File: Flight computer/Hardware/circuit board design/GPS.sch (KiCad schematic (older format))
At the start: 5 parts, among them U12 MAX2659ELT+, U13 SAFEB1G57KE0F00, U4 MAX-M8C

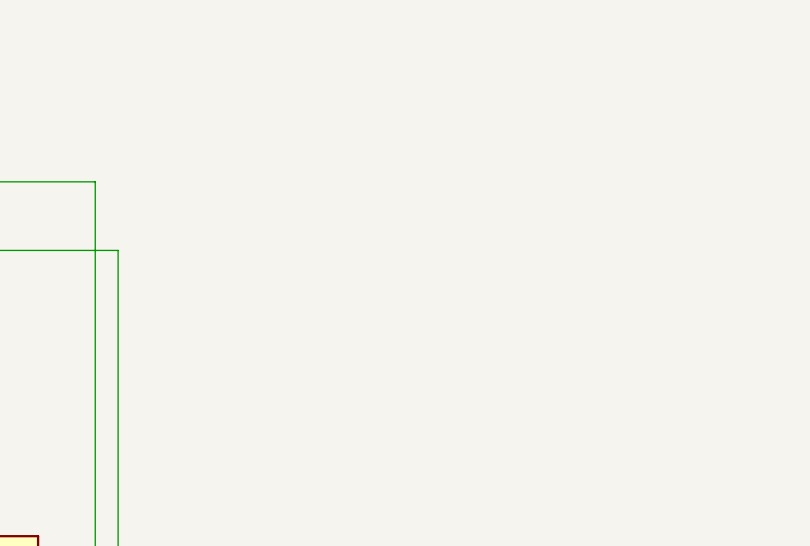
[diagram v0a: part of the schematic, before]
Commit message: moved gps antenna coax connection to right page
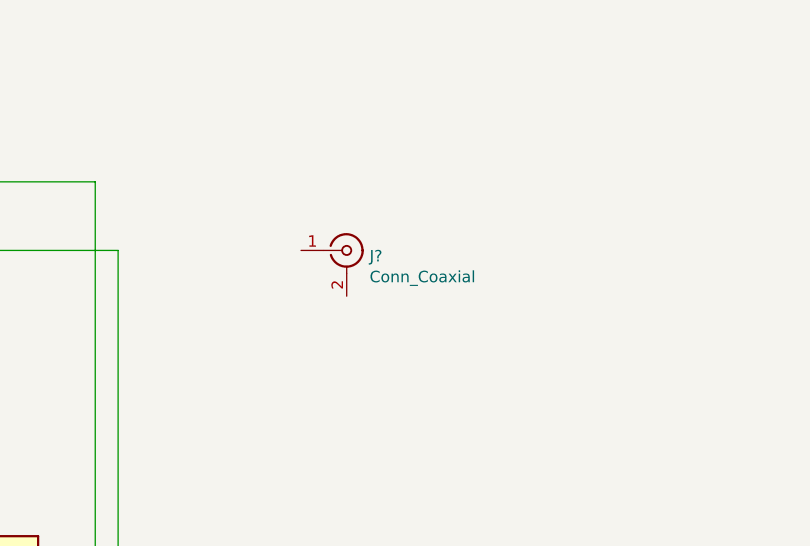
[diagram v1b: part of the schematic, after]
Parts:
- added J?: Conn_Coaxial, Connector_Coaxial:U.FL_Hirose_U.FL-R-SMT-1_Vertical, symbol Connector:Conn_Coaxial
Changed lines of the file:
@@
 Wire Wire Line
 	1800 1900 2100 1900
+$Comp
+L Connector:Conn_Coaxial J?
+U 1 1 5D772D40
+P 7900 2200
+AR Path="/5D5B17D8/5D772D40" Ref="J?"  Part="1"
+AR Path="/5D5B165E/5D772D40" Ref="J?"  Part="1"
+F 0 "J?" H 8000 2175 50  0000 L CNN
+F 1 "Conn_Coaxial" H 8000 2084 50  0000 L CNN
+F 2 "Connector_Coaxial:U.FL_Hirose_U.FL-R-SMT-1_Vertical" H 7900 2200 50  0001 C CNN
+F 3 " ~" H 7900 2200 50  0001 C CNN
+	1    7900 2200
+	1    0    0    -1
+$EndComp
 $EndSCHEMATC

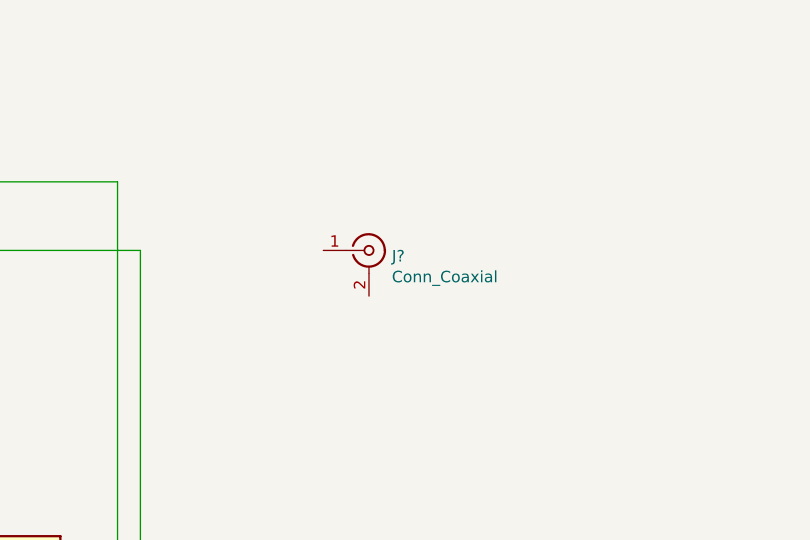
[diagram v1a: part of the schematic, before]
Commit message: added in the RF front end, exactly as stated in AN904
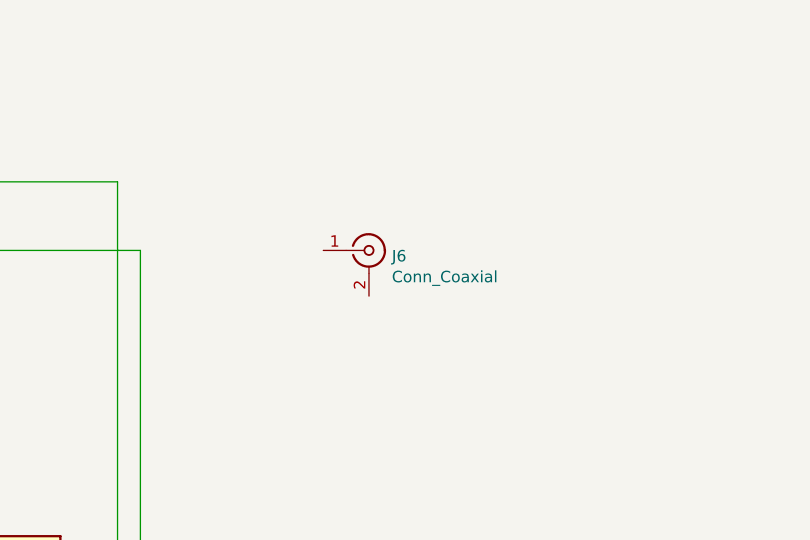
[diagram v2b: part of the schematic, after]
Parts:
- gave numbers to parts that had none: 1
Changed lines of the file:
@@
 P 7900 2200
 AR Path="/5D5B17D8/5D772D40" Ref="J?"  Part="1"
-AR Path="/5D5B165E/5D772D40" Ref="J?"  Part="1"
-F 0 "J?" H 8000 2175 50  0000 L CNN
+AR Path="/5D5B165E/5D772D40" Ref="J6"  Part="1"
+F 0 "J6" H 8000 2175 50  0000 L CNN
 F 1 "Conn_Coaxial" H 8000 2084 50  0000 L CNN
 F 2 "Connector_Coaxial:U.FL_Hirose_U.FL-R-SMT-1_Vertical" H 7900 2200 50  0001 C CNN

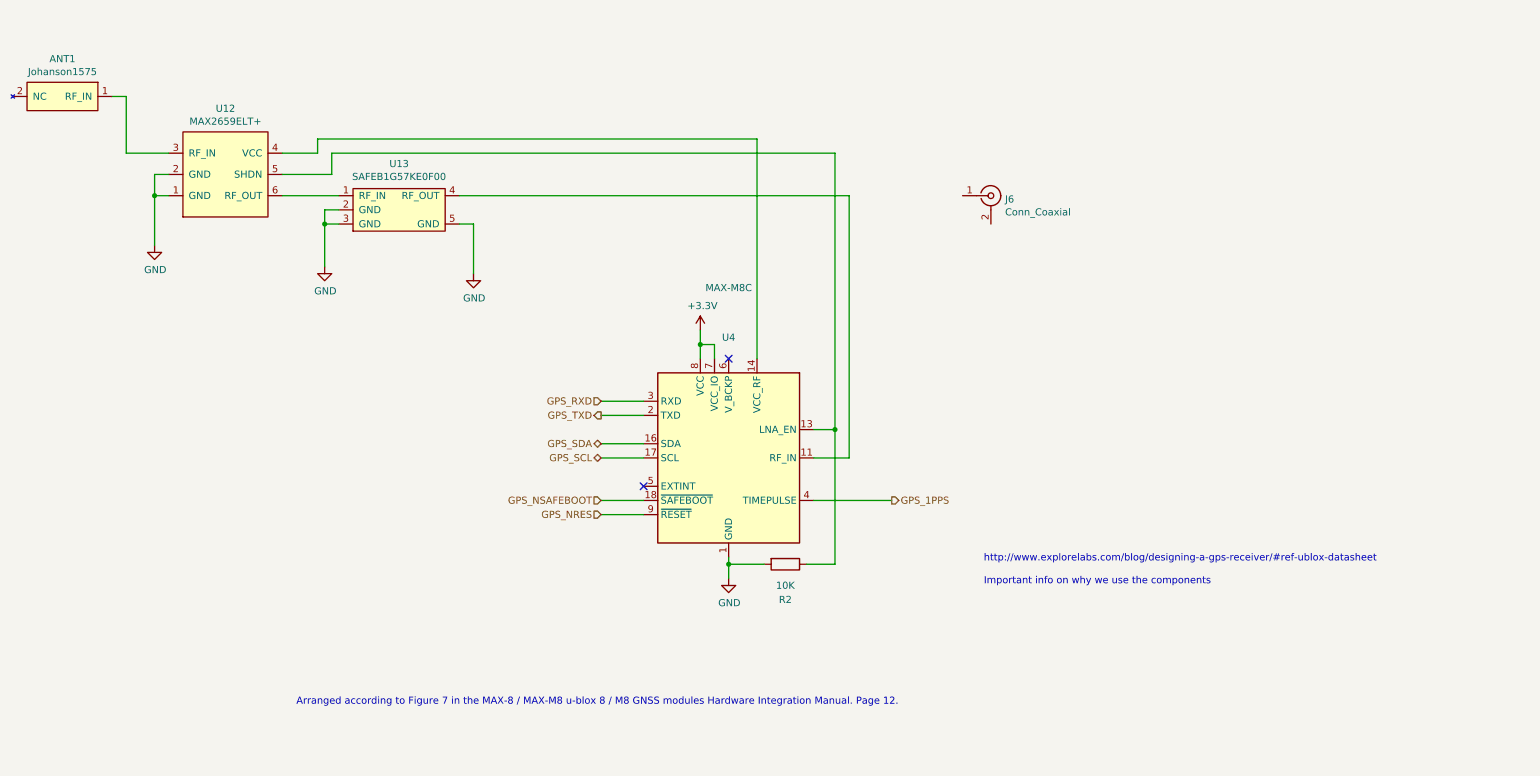
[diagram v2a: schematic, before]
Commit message: put in a UFL connector in place of the Active GPS antenna
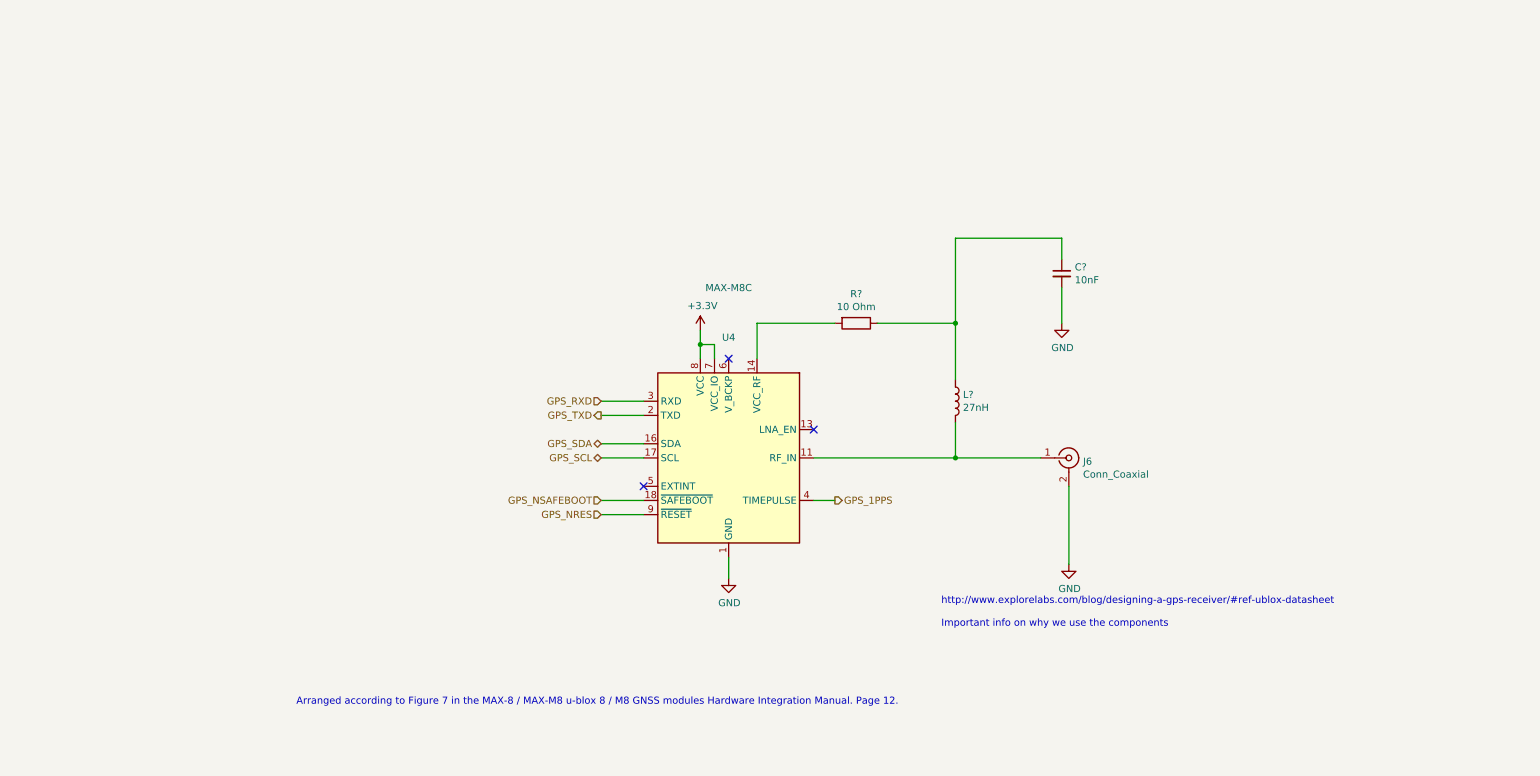
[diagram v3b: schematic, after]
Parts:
- removed ANT1: Johanson1575, pico_tracker:Johanson1575, symbol flight-computer:ICSSPicoTracker_Johanson1575
- removed R2: 10K, Resistor_SMD:R_0603_1608Metric, symbol Device:R
- removed U12: MAX2659ELT+, pico_tracker:uDFN-6_1.0x1.5mm_P0.5mm, symbol flight-computer:ICSSPicoTracker_MAX2659ELT+
- removed U13: SAFEB1G57KE0F00, pico_tracker:Murata SAFE, symbol flight-computer:ICSSPicoTracker_SAFEB1G57KE0F00
- added C?: 10nF, symbol Device:C_Small
- added L?: 27nH, symbol Device:L
- added R?: 10 Ohm, symbol Device:R
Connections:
- net GND: now also J6.2 (Ext), C?.2
- net at U4.14 (VCC_RF): now also R?.2
- net at U4.11 (RF_IN): now also J6.1 (In), L?.2
- new net: C?.1, L?.1, R?.1
- no-connect marks 2 -> 3
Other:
- moved on the sheet: J6
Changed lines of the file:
@@
 Comment4 ""
 $EndDescr
+Text HLabel 6800 4350 2    50   Output ~ 0
+GPS_1PPS
+Text Notes 3000 5800 0    50   ~ 0
+Arranged according to Figure 7 in the MAX-8 / MAX-M8 u-blox 8 / M8 GNSS modules Hardware Integration Manual. Page 12.
+Text Notes 7550 5250 0    50   ~ 0
+http://www.explorelabs.com/blog/designing-a-gps-receiver/#ref-ublox-datasheet\n\nImportant info on why we use the components\n
 $Comp
-L flight-computer:ICSSPicoTracker_SAFEB1G57KE0F00 U13
-U 1 1 5D44BB5C
-P 3400 2450
-F 0 "U13" H 3725 2925 50  0000 C CNN
-F 1 "SAFEB1G57KE0F00" H 3725 2834 50  0000 C CNN
-F 2 "pico_tracker:Murata SAFE" H 3400 2450 50  0001 C CNN
-F 3 "https://www.murata.com/en-eu/products/productdata/8797690593310/DS-SAFEB1G57KE0F00.pdf?1453347007000" H 3400 2450 50  0001 C CNN
-F 4 "https://www.rf-microwave.com/en/murata/safeb1g57ke0f00/1575-5-mhz-band-pass-saw/fw-safeb1g57/" H 3400 2450 50  0001 C CNN "Purchase link"
-	1    3400 2450
+L power:+3.3V #PWR010
+U 1 1 5D692740
+P 5850 3150
+F 0 "#PWR010" H 5850 3000 50  0001 C CNN
+F 1 "+3.3V" H 5865 3323 50  0000 C CNN
+F 2 "" H 5850 3150 50  0001 C CNN
+F 3 "" H 5850 3150 50  0001 C CNN
+	1    5850 3150
 	1    0    0    -1
 $EndComp
 $Comp
-L power:GND #PWR053
-U 1 1 5D459323
-P 3200 2700
-F 0 "#PWR053" H 3200 2450 50  0001 C CNN
-F 1 "GND" H 3205 2527 50  0000 C CNN
-F 2 "" H 3200 2700 50  0001 C CNN
-F 3 "" H 3200 2700 50  0001 C CNN
-	1    3200 2700
-	1    0    0    -1
-$EndComp
-$Comp
-L power:GND #PWR058
-U 1 1 5D459A04
-P 4250 2750
-F 0 "#PWR058" H 4250 2500 50  0001 C CNN
-F 1 "GND" H 4255 2577 50  0000 C CNN
-F 2 "" H 4250 2750 50  0001 C CNN
-F 3 "" H 4250 2750 50  0001 C CNN
-	1    4250 2750
+L power:GND #PWR011
+U 1 1 5D67FE0F
+P 6050 4900
+F 0 "#PWR011" H 6050 4650 50  0001 C CNN
+F 1 "GND" H 6055 4727 50  0000 C CNN
+F 2 "" H 6050 4900 50  0001 C CNN
+F 3 "" H 6050 4900 50  0001 C CNN
+	1    6050 4900
 	1    0    0    -1
 $EndComp
 Wire Wire Line
-	4150 2400 4250 2400
+	5850 3150 5850 3250
 Wire Wire Line
-	4250 2400 4250 2750
+	5950 3250 5850 3250
+Text HLabel 5150 3750 0    50   Output ~ 0
+GPS_TXD
+Text HLabel 5150 3650 0    50   Input ~ 0
+GPS_RXD
+Text HLabel 5150 4050 0    50   BiDi ~ 0
+GPS_SCL
+Text HLabel 5150 3950 0    50   BiDi ~ 0
+GPS_SDA
+Text HLabel 5150 4350 0    50   Input ~ 0
+GPS_NSAFEBOOT
+Text HLabel 5150 4450 0    50   Input ~ 0
+GPS_NRES
+$Comp
+L Connector:Conn_Coaxial J?
+U 1 1 5D772D40
+P 8450 4050
+AR Path="/5D5B17D8/5D772D40" Ref="J?"  Part="1"
+AR Path="/5D5B165E/5D772D40" Ref="J6"  Part="1"
+F 0 "J6" H 8550 4025 50  0000 L CNN
+F 1 "Conn_Coaxial" H 8550 3934 50  0000 L CNN
+F 2 "Connector_Coaxial:U.FL_Hirose_U.FL-R-SMT-1_Vertical" H 8450 4050 50  0001 C CNN
+F 3 " ~" H 8450 4050 50  0001 C CNN
+	1    8450 4050
+	1    0    0    -1
+$EndComp
 Wire Wire Line
-	3300 2300 3200 2300
+	8450 4800 8450 4250
+$Comp
+L power:GND #PWR?
+U 1 1 5D7B7248
+P 8450 4800
+F 0 "#PWR?" H 8450 4550 50  0001 C CNN
+F 1 "GND" H 8455 4627 50  0000 C CNN
+F 2 "" H 8450 4800 50  0001 C CNN
+F 3 "" H 8450 4800 50  0001 C CNN
+	1    8450 4800
+	1    0    0    -1
+$EndComp
+Connection ~ 7650 4050
 Wire Wire Line
-	3200 2300 3200 2400
+	7650 4050 8250 4050
+$Comp
+L Device:L L?
+U 1 1 5D7B7FB8
+P 7650 3650
+F 0 "L?" H 7703 3696 50  0000 L CNN
+F 1 "27nH" H 7703 3605 50  0000 L CNN
+F 2 "" H 7650 3650 50  0001 C CNN
+F 3 "~" H 7650 3650 50  0001 C CNN
+	1    7650 3650
+	1    0    0    -1
+$EndComp
 Wire Wire Line
-	3300 2400 3200 2400
-Connection ~ 3200 2400
+	7650 3800 7650 4050
+Connection ~ 5850 3250
 Wire Wire Line
-	3200 2400 3200 2700
+	5150 4450 5450 4450
 Wire Wire Line
-	3250 2050 3250 1900
-Text HLabel 7200 4350 2    50   Output ~ 0
-GPS_1PPS
-Text Notes 3000 5800 0    50   ~ 0
-Arranged according to Figure 7 in the MAX-8 / MAX-M8 u-blox 8 / M8 GNSS modules Hardware Integration Manual. Page 12.
+	5850 3250 5850 3350
 Wire Wire Line
-	3250 1900 6800 1900
-Text Notes 7850 4950 0    50   ~ 0
-http://www.explorelabs.com/blog/designing-a-gps-receiver/#ref-ublox-datasheet\n\nImportant info on why we use the components\n
+	5950 3350 5950 3250
+NoConn ~ 6050 3350
 NoConn ~ 5450 4250
+Wire Wire Line
+	6650 4350 6800 4350
+Wire Wire Line
+	5450 3650 5150 3650
+Wire Wire Line
+	5150 3750 5450 3750
+Wire Wire Line
+	5450 4350 5150 4350
+Wire Wire Line
+	5150 4050 5450 4050
+Wire Wire Line
+	5450 3950 5150 3950
+NoConn ~ 6650 3850
+Wire Wire Line
+	6650 4050 7650 4050
+Wire Wire Line
+	6050 4750 6050 4900
 $Comp
 L RF_GPS:MAX-M8C U4
@@
 $EndComp
 Wire Wire Line
-	6300 4800 6050 4800
+	6250 3350 6250 3100
+Wire Wire Line
+	6250 3100 6800 3100
+Wire Wire Line
+	7650 3100 7650 3500
 $Comp
-L Device:R R2
-U 1 1 5D69D778
-P 6450 4800
-F 0 "R2" V 6700 4800 50  0000 C CNN
-F 1 "10K" V 6600 4800 50  0000 C CNN
-F 2 "Resistor_SMD:R_0603_1608Metric" V 6380 4800 50  0001 C CNN
-F 3 "~" H 6450 4800 50  0001 C CNN
-	1    6450 4800
+L Device:R R?
+U 1 1 5D7B91DB
+P 6950 3100
+F 0 "R?" V 6743 3100 50  0000 C CNN
+F 1 "10 Ohm" V 6834 3100 50  0000 C CNN
+F 2 "" V 6880 3100 50  0001 C CNN
+F 3 "~" H 6950 3100 50  0001 C CNN
+	1    6950 3100
 	0    1    1    0
 $EndComp
 Wire Wire Line
-	6050 4800 6050 4750
-Connection ~ 6050 4800
-Connection ~ 6800 3850
+	7100 3100 7650 3100
 Wire Wire Line
-	6800 4800 6600 4800
-Wire Wire Line
-	6800 3850 6800 4800
-Wire Wire Line
-	6050 4900 6050 4800
-Wire Wire Line
-	6650 4350 7200 4350
+	7650 3100 7650 2500
+Connection ~ 7650 3100
 $Comp
-L power:+3.3V #PWR010
-U 1 1 5D692740
-P 5850 3150
-F 0 "#PWR010" H 5850 3000 50  0001 C CNN
-F 1 "+3.3V" H 5865 3323 50  0000 C CNN
-F 2 "" H 5850 3150 50  0001 C CNN
-F 3 "" H 5850 3150 50  0001 C CNN
-	1    5850 3150
+L power:GND #PWR?
+U 1 1 5D7B9CCD
+P 8400 3100
+F 0 "#PWR?" H 8400 2850 50  0001 C CNN
+F 1 "GND" H 8405 2927 50  0000 C CNN
+F 2 "" H 8400 3100 50  0001 C CNN
+F 3 "" H 8400 3100 50  0001 C CNN
+	1    8400 3100
 	1    0    0    -1
 $EndComp
 Wire Wire Line
-	6800 1900 6800 3850
+	8400 2500 8400 2650
 Wire Wire Line
-	6800 3850 6650 3850
+	7650 2500 8400 2500
 $Comp
-L power:GND #PWR011
-U 1 1 5D67FE0F
-P 6050 4900
-F 0 "#PWR011" H 6050 4650 50  0001 C CNN
-F 1 "GND" H 6055 4727 50  0000 C CNN
-F 2 "" H 6050 4900 50  0001 C CNN
-F 3 "" H 6050 4900 50  0001 C CNN
-	1    6050 4900
+L Device:C_Small C?
+U 1 1 5D7BADC4
+P 8400 2750
+F 0 "C?" H 8492 2796 50  0000 L CNN
+F 1 "10nF" H 8492 2705 50  0000 L CNN
+F 2 "" H 8400 2750 50  0001 C CNN
+F 3 "~" H 8400 2750 50  0001 C CNN
+	1    8400 2750
 	1    0    0    -1
 $EndComp
 Wire Wire Line
-	6900 4050 6650 4050
-Wire Wire Line
-	4150 2200 6900 2200
-Wire Wire Line
-	6900 2200 6900 4050
-Wire Wire Line
-	3150 1800 3150 1900
-Wire Wire Line
-	6250 3350 6250 1800
-Wire Wire Line
-	6250 1800 3150 1800
-Wire Wire Line
-	5850 3150 5850 3250
-Wire Wire Line
-	5950 3350 5950 3250
-Wire Wire Line
-	5950 3250 5850 3250
-Connection ~ 5850 3250
-Wire Wire Line
-	5850 3250 5850 3350
-NoConn ~ 6050 3350
-$Comp
-L power:GND #PWR052
-U 1 1 5D458C8C
-P 2000 2550
-F 0 "#PWR052" H 2000 2300 50  0001 C CNN
-F 1 "GND" H 2005 2377 50  0000 C CNN
-F 2 "" H 2000 2550 50  0001 C CNN
-F 3 "" H 2000 2550 50  0001 C CNN
-	1    2000 2550
-	1    0    0    -1
-$EndComp
-Wire Wire Line
-	2000 2050 2000 2200
-Connection ~ 2000 2200
-Wire Wire Line
-	2000 2200 2000 2550
-Wire Wire Line
-	2100 2050 2000 2050
-Wire Wire Line
-	2100 2200 2000 2200
-$Comp
-L flight-computer:ICSSPicoTracker_MAX2659ELT+ U12
-U 1 1 5D44B218
-P 2200 2350
-F 0 "U12" H 2500 3115 50  0000 C CNN
-F 1 "MAX2659ELT+" H 2500 3024 50  0000 C CNN
-F 2 "pico_tracker:uDFN-6_1.0x1.5mm_P0.5mm" H 2200 2350 50  0001 C CNN
-F 3 "https://datasheets.maximintegrated.com/en/ds/MAX2659.pdf" H 2200 2350 50  0001 C CNN
-F 4 "https://www.mouser.co.uk/ProductDetail/Maxim-Integrated/MAX2659ELT+T?qs=GxOUx7aO6nyMDHP%2F45gvTg==" H 2200 2350 50  0001 C CNN "Purchase link"
-	1    2200 2350
-	1    0    0    -1
-$EndComp
-Wire Wire Line
-	3150 1900 2900 1900
-Wire Wire Line
-	2900 2050 3250 2050
-Wire Wire Line
-	3300 2200 2900 2200
-Wire Wire Line
-	1800 1500 1700 1500
-$Comp
-L flight-computer:ICSSPicoTracker_Johanson1575 ANT1
-U 1 1 5D521711
-P 1300 1500
-AR Path="/5D521711" Ref="ANT1"  Part="1"
-AR Path="/5D2ABE03/5D521711" Ref="ANT1"  Part="1"
-AR Path="/5D5B165E/5D521711" Ref="ANT1"  Part="1"
-F 0 "ANT1" H 1250 1765 50  0000 C CNN
-F 1 "Johanson1575" H 1250 1674 50  0000 C CNN
-F 2 "pico_tracker:Johanson1575" H 1300 1500 50  0001 C CNN
-F 3 "https://www.mouser.co.uk/datasheet/2/611/JTI_Antenna-1575AT43A40_2006-09-399627.pdf" H 1300 1500 50  0001 C CNN
-F 4 "0.753" H 1300 1500 50  0001 C CNN "Cost"
-F 5 "https://www.mouser.co.uk/ProductDetail/Johanson-Technology/1575AT43A0040E?qs=qF3SSroohZWOIHwrK8wTew%3D%3D" H 1300 1500 50  0001 C CNN "Purchase link"
-	1    1300 1500
-	-1   0    0    -1
-$EndComp
-Wire Wire Line
-	5450 3950 5150 3950
-Text HLabel 5150 3750 0    50   Output ~ 0
-GPS_TXD
-Text HLabel 5150 3650 0    50   Input ~ 0
-GPS_RXD
-Text HLabel 5150 4050 0    50   BiDi ~ 0
-GPS_SCL
-Text HLabel 5150 3950 0    50   BiDi ~ 0
-GPS_SDA
-Text HLabel 5150 4350 0    50   Input ~ 0
-GPS_NSAFEBOOT
-Text HLabel 5150 4450 0    50   Input ~ 0
-GPS_NRES
-Wire Wire Line
-	5450 3650 5150 3650
-Wire Wire Line
-	5450 4350 5150 4350
-Wire Wire Line
-	5150 3750 5450 3750
-Wire Wire Line
-	5150 4450 5450 4450
-Wire Wire Line
-	5150 4050 5450 4050
-Wire Wire Line
-	1800 1900 1800 1500
-Wire Wire Line
-	1800 1900 2100 1900
-$Comp
-L Connector:Conn_Coaxial J?
-U 1 1 5D772D40
-P 7900 2200
-AR Path="/5D5B17D8/5D772D40" Ref="J?"  Part="1"
-AR Path="/5D5B165E/5D772D40" Ref="J6"  Part="1"
-F 0 "J6" H 8000 2175 50  0000 L CNN
-F 1 "Conn_Coaxial" H 8000 2084 50  0000 L CNN
-F 2 "Connector_Coaxial:U.FL_Hirose_U.FL-R-SMT-1_Vertical" H 7900 2200 50  0001 C CNN
-F 3 " ~" H 7900 2200 50  0001 C CNN
-	1    7900 2200
-	1    0    0    -1
-$EndComp
+	8400 2850 8400 3100
 $EndSCHEMATC
